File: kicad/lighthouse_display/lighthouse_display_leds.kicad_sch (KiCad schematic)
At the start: 105 parts

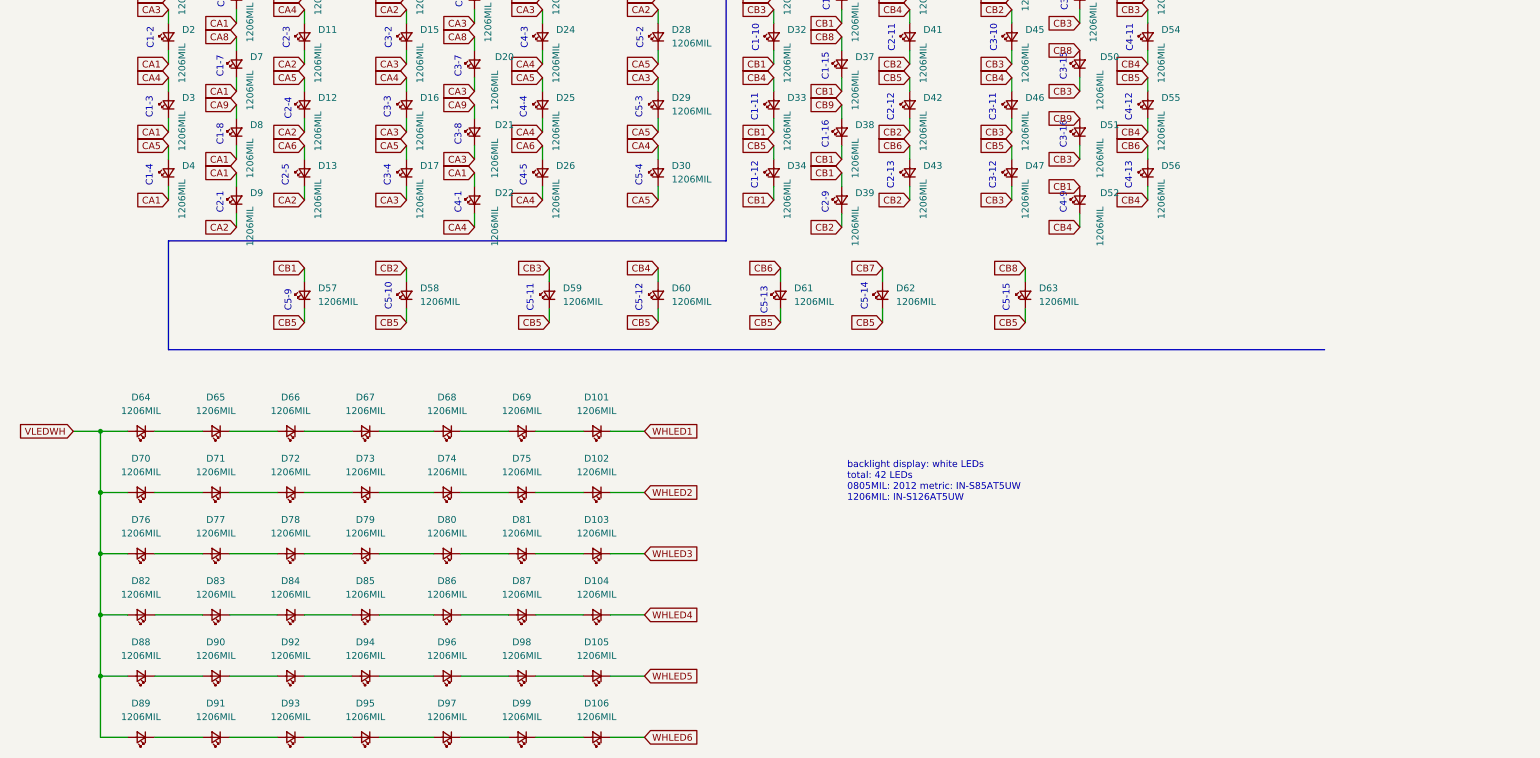
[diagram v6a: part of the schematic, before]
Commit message: ordererd lighthouse display
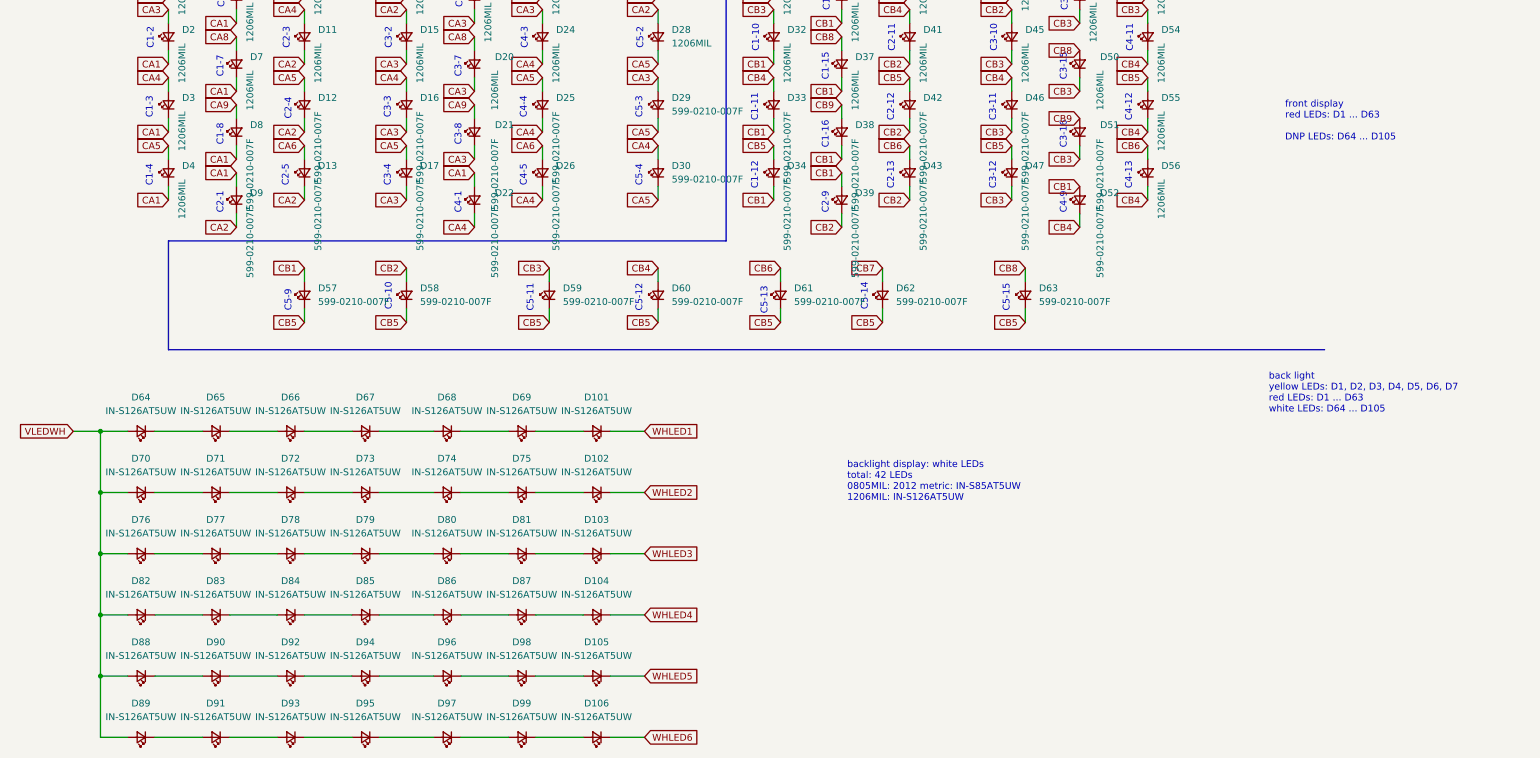
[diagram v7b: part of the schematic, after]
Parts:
- D101, D102, D103, D104, D105, D106, D64, D65, D66, D67, D68, D69, D70, D71, D72, D73, D74, D75, D76, D77, D78, D79, D80, D81, D82, D83, D84, D85, D86, D87, D88, D89, D90, D91, D92, D93, D94, D95, D96, D97, D98, D99: value 1206MIL -> IN-S126AT5UW
- D12, D13, D16, D17, D21, D22, D25, D26, D29, D30, D33, D34, D38, D39, D42, D43, D46, D47, D51, D52, D57, D58, D59, D60, D61, D62, D63, D8, D9: value 1206MIL -> 599-0210-007F
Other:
- note added: "back light yellow LEDs: D1, D2, D3, D4, D5, D6, D7 red LEDs: D1 ... D63 white LEDs: D64 ... D105"
- note added: "front display red LEDs: D1 ... D63 DNP LEDs: D64 ... D105"
